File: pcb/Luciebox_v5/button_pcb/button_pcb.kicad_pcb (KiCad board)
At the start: 2 copper layers, 78 x 100 mm, 23 parts, among them T1 terminal_8x1, T2 terminal_8x1, T3 terminal_8x1, T4 terminal_2x1, U1 8X8PADS

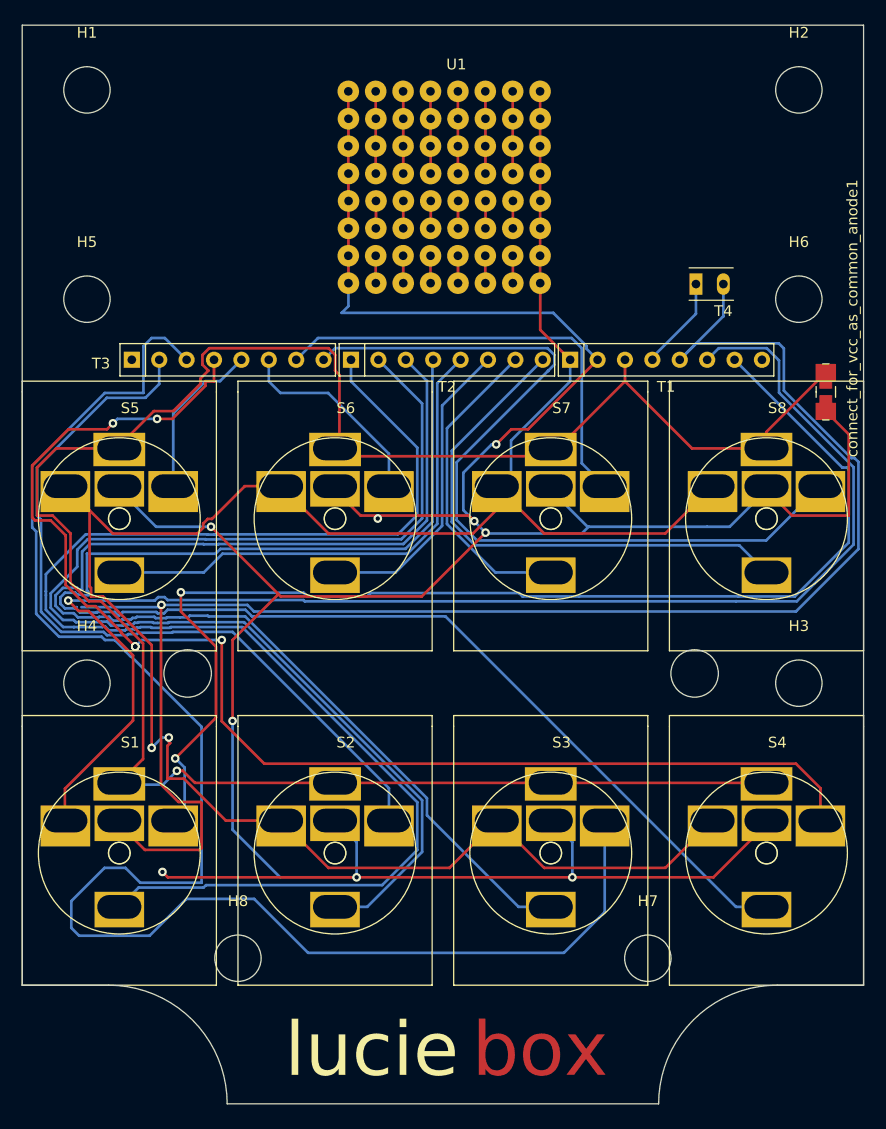
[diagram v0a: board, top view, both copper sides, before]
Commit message: Start pcb v5 with feedback from v4
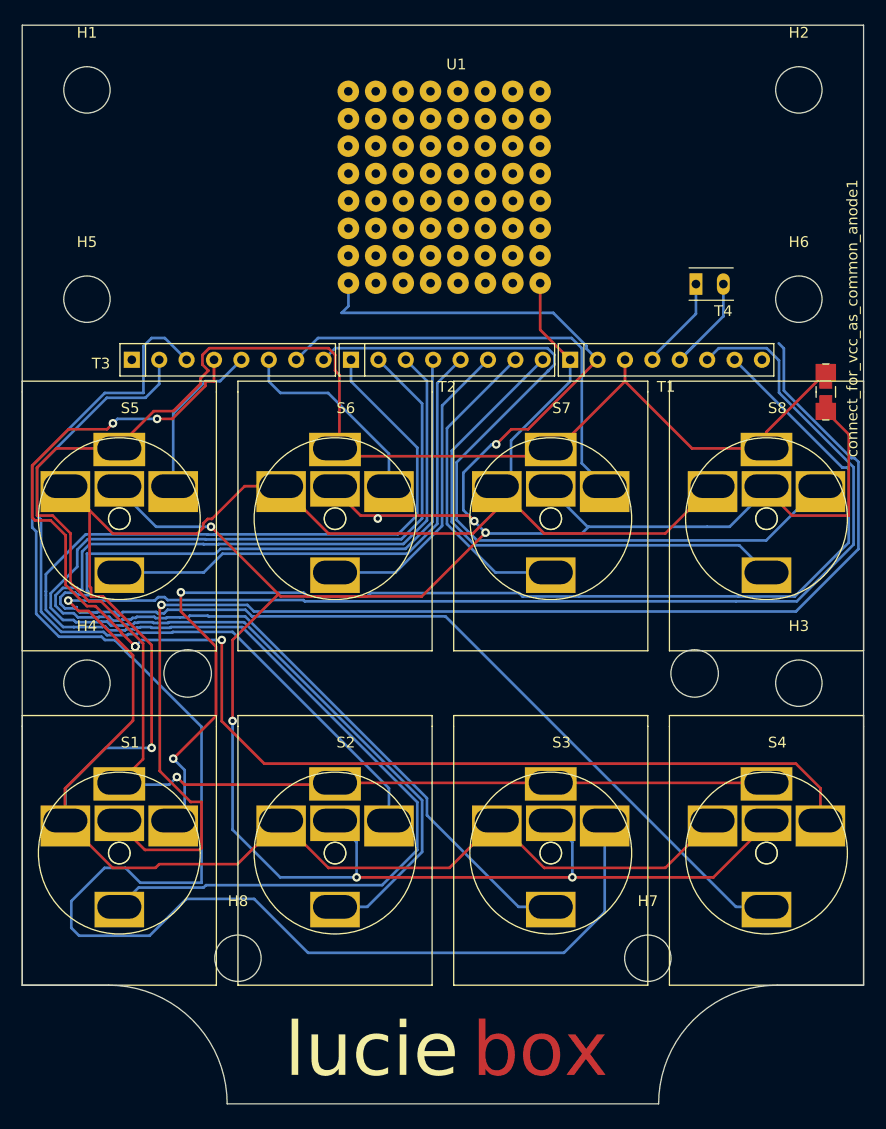
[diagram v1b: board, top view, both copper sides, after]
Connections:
- S1 pad 1: Net-(BT1-Pad1) -> Net-(T1-Pad8)
- T1 pad 8: unconnected-(T1-Pad8) -> Net-(T1-Pad8)
- U1 pad 25: Net-(U1-Pad25) -> unconnected-(U1-Pad25)
- U1 pad 26: Net-(U1-Pad25) -> unconnected-(U1-Pad26)
- U1 pad 27: Net-(U1-Pad27) -> unconnected-(U1-Pad27)
- U1 pad 28: Net-(U1-Pad27) -> unconnected-(U1-Pad28)
- U1 pad 29: Net-(U1-Pad29) -> unconnected-(U1-Pad29)
- U1 pad 30: Net-(U1-Pad29) -> Net-(U1-Pad30)
- U1 pad 31: Net-(U1-Pad29) -> Net-(U1-Pad30)
- U1 pad 32: Net-(U1-Pad29) -> Net-(U1-Pad30)
- U1 pad 33: Net-(U1-Pad33) -> unconnected-(U1-Pad33)
- U1 pad 34: Net-(U1-Pad33) -> unconnected-(U1-Pad34)
- U1 pad 35: Net-(U1-Pad35) -> unconnected-(U1-Pad35)
- U1 pad 36: Net-(U1-Pad35) -> unconnected-(U1-Pad36)
- U1 pad 37: Net-(U1-Pad38) -> unconnected-(U1-Pad37)
- U1 pad 41: Net-(U1-Pad41) -> unconnected-(U1-Pad41)
- U1 pad 42: Net-(U1-Pad41) -> unconnected-(U1-Pad42)
- U1 pad 43: Net-(U1-Pad43) -> unconnected-(U1-Pad43)
- U1 pad 44: Net-(U1-Pad43) -> unconnected-(U1-Pad44)
- U1 pad 45: Net-(U1-Pad45) -> unconnected-(U1-Pad45)
- U1 pad 46: Net-(U1-Pad45) -> Net-(U1-Pad46)
- U1 pad 47: Net-(U1-Pad45) -> Net-(U1-Pad46)
- U1 pad 48: Net-(U1-Pad45) -> Net-(U1-Pad46)
- U1 pad 49: Net-(U1-Pad49) -> unconnected-(U1-Pad49)
- U1 pad 50: Net-(U1-Pad49) -> unconnected-(U1-Pad50)
- U1 pad 51: Net-(U1-Pad51) -> unconnected-(U1-Pad51)
- U1 pad 52: Net-(U1-Pad51) -> unconnected-(U1-Pad52)
- U1 pad 53: Net-(U1-Pad53) -> unconnected-(U1-Pad53)
- U1 pad 54: Net-(U1-Pad53) -> Net-(U1-Pad54)
- U1 pad 55: Net-(U1-Pad53) -> Net-(U1-Pad54)
- U1 pad 56: Net-(U1-Pad53) -> Net-(U1-Pad54)
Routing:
- net Net-(BT1-Pad1): track 150.7 -> 10.9 mm, vias 1 -> 0
- net Net-(S1-Pad2): track 129.0 -> 0.00 mm, vias 1 -> 0
- net GND: track 206.6 -> 334.5 mm
- net Net-(T1-Pad8): track 0.00 -> 124.5 mm, vias 0 -> 1
- net VCC: track 286.2 -> 250.2 mm, vias 9 -> 8
- net Net-(U1-Pad45): track 7.63 -> 0.00 mm
- net Net-(U1-Pad38): track 7.63 -> 0.00 mm
- net Net-(U1-Pad29): track 7.63 -> 0.00 mm
- net Net-(U1-Pad21): track 7.63 -> 0.00 mm
- net Net-(U1-Pad13): track 7.63 -> 0.00 mm
- net Net-(U1-Pad53): track 7.63 -> 0.00 mm
- net Net-(U1-Pad19): track 2.81 -> 0.00 mm
- net Net-(U1-Pad41): track 2.55 -> 0.00 mm
- net Net-(U1-Pad33): track 2.55 -> 0.00 mm
- net Net-(U1-Pad25): track 2.55 -> 0.00 mm
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
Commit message: Pcb V5
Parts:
- removed H1, H2, H3, H4: MountingHole, Luciebox_components:MountingHole_4.3mm_M4
- removed U1: 8X8PADS, Luciebox_components:8X8PADS_100mil
- added JPowerBankAsBattery1: USB_B_Mini, Luciebox_components:usb_mini_Molex-0548190519, F.Cu at (58.5, 28.0)
- S1, S2, S3, S4: footprint Luciebox_components:button_LAZ16-11_big_holes -> Luciebox_components:button_square_17.5x17.5mm_big_holes
- T4, connect_for_vcc_as_common_anode1: moved to B.Cu
- moved S5 31.0 mm to (9.00, 74.5)
- moved S6 31.0 mm to (29.0, 74.5)
- moved S7 31.0 mm to (49.0, 74.5)
- moved S8 31.0 mm to (69.0, 74.5)
- moved S1 23.5 mm to (9.00, 51.0)
- moved S2 23.5 mm to (29.0, 51.0)
- moved S3 23.5 mm to (49.0, 51.0)
- moved S4 23.5 mm to (69.0, 51.0)
- moved T4 17.3 mm to (48.6, 29.6)
- moved T1 7.00 mm to (59.7, 38.0)
- moved T2 7.00 mm to (39.4, 38.0)
- moved T3 7.00 mm to (19.1, 38.0)
- moved H5 7.00 mm to (6.00, 32.4)
- moved H6 7.00 mm to (72.0, 32.4)
- moved connect_for_vcc_as_common_anode1 6.26 mm to (74.3, 40.3)
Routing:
- net GND: track 334.5 -> 172.3 mm, vias 2 -> 1
- net Net-(S1-Pad5): track 133.4 -> 30.7 mm
- net Net-(S3-Pad3): track 150.3 -> 53.1 mm
- net Net-(S4-Pad5): track 134.0 -> 40.7 mm
- net Net-(S3-Pad5): track 115.1 -> 27.3 mm
- net Net-(S2-Pad5): track 113.1 -> 26.4 mm
- net Net-(S1-Pad2): track 0.00 -> 72.3 mm
- net Net-(S5-Pad5): track 47.5 -> 104.1 mm
- net Net-(S4-Pad3): track 121.2 -> 169.5 mm, vias 5 -> 0
- net Net-(S5-Pad3): track 15.1 -> 63.1 mm
- net Net-(S2-Pad3): track 72.6 -> 28.1 mm
- net Net-(S1-Pad3): track 111.0 -> 77.2 mm, vias 2 -> 0
- net Net-(BT1-Pad2): track 8.69 -> 42.1 mm
- net Net-(S8-Pad5): track 49.6 -> 82.3 mm
- net Net-(S1-Pad1): track 124.5 -> 93.0 mm, vias 1 -> 0
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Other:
- board size 78 x 100 mm -> 78 x 72 mm
- board text added: "button board v3.0 2023-02 a Nonkel Lode luciebox extension putting extra pret in the bak buttons: laz16-11"
- board text removed: "button board v2.0 2022-11 a Nonkel Lode luciebox extension putting extra pret in the bak buttons: laz16-11"
